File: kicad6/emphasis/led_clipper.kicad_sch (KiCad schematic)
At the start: 16 parts, among them U2 TL072

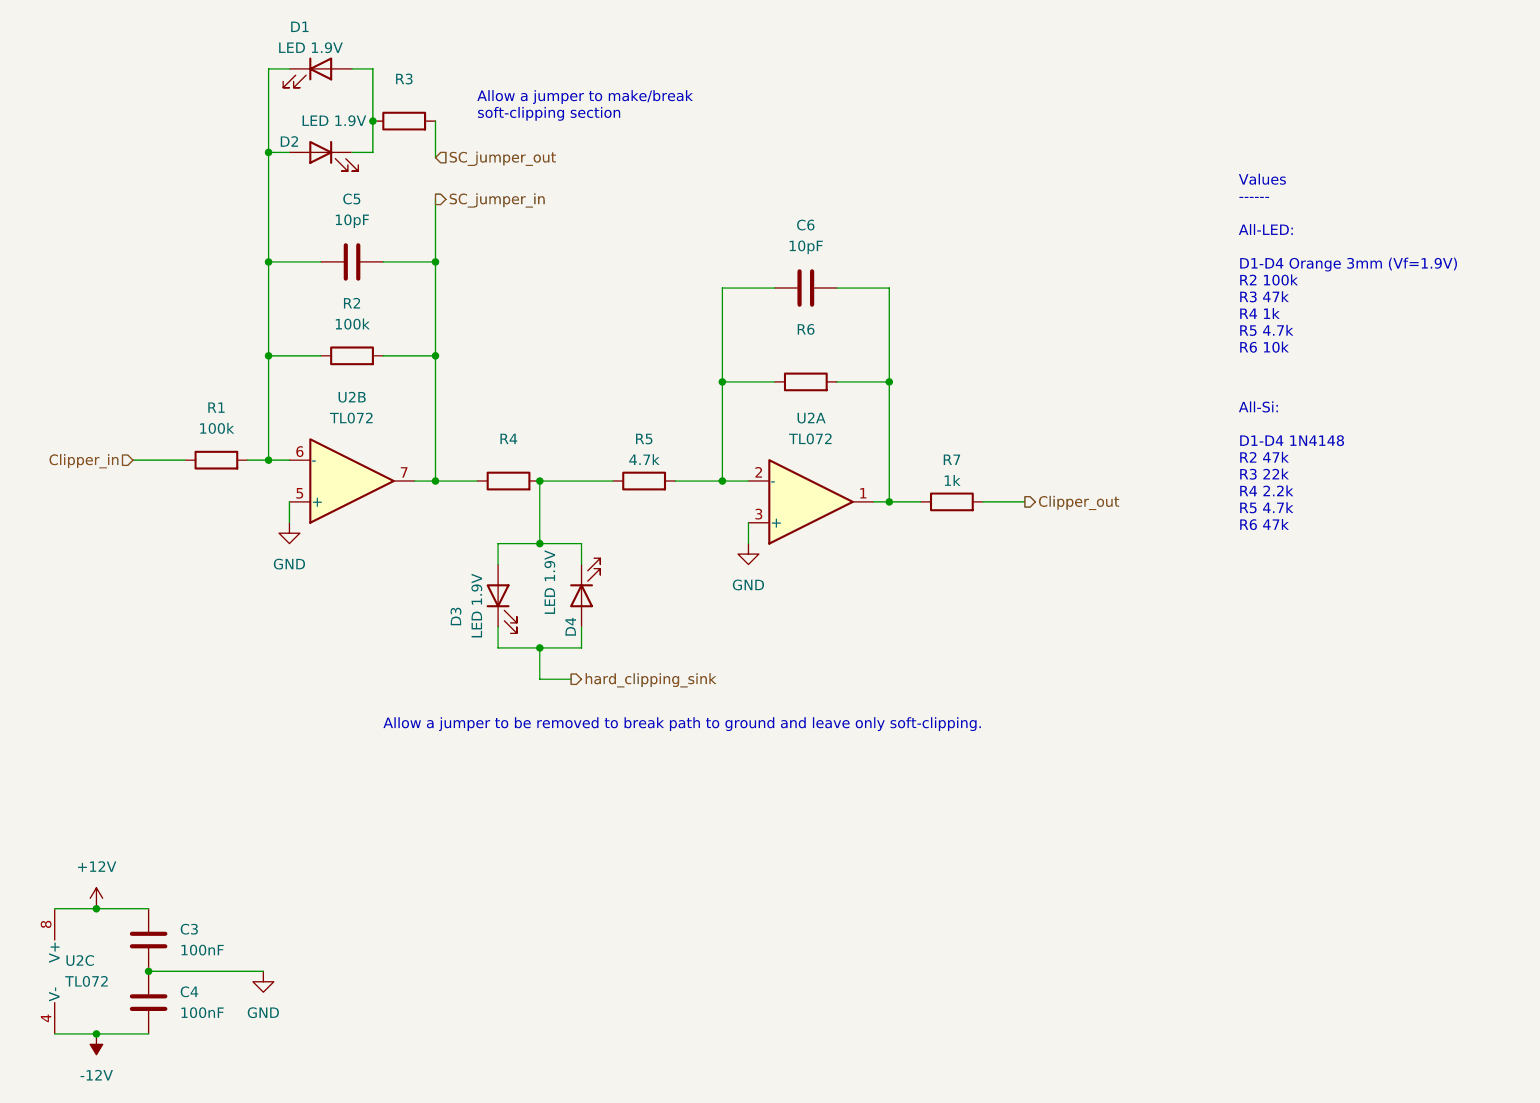
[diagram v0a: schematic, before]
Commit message: Emphasis: flipped board, take 1
Not entirely happy with the way this is going, might start again.

Basically I messed up the orientation of the main board relative to
the control board: to avoid having the patch_sm stick out the side,
parts need to be mounted on the "back" of main board. But this flips
the orientation of patch_sm and ICs, so everything needs to be
re-routed.
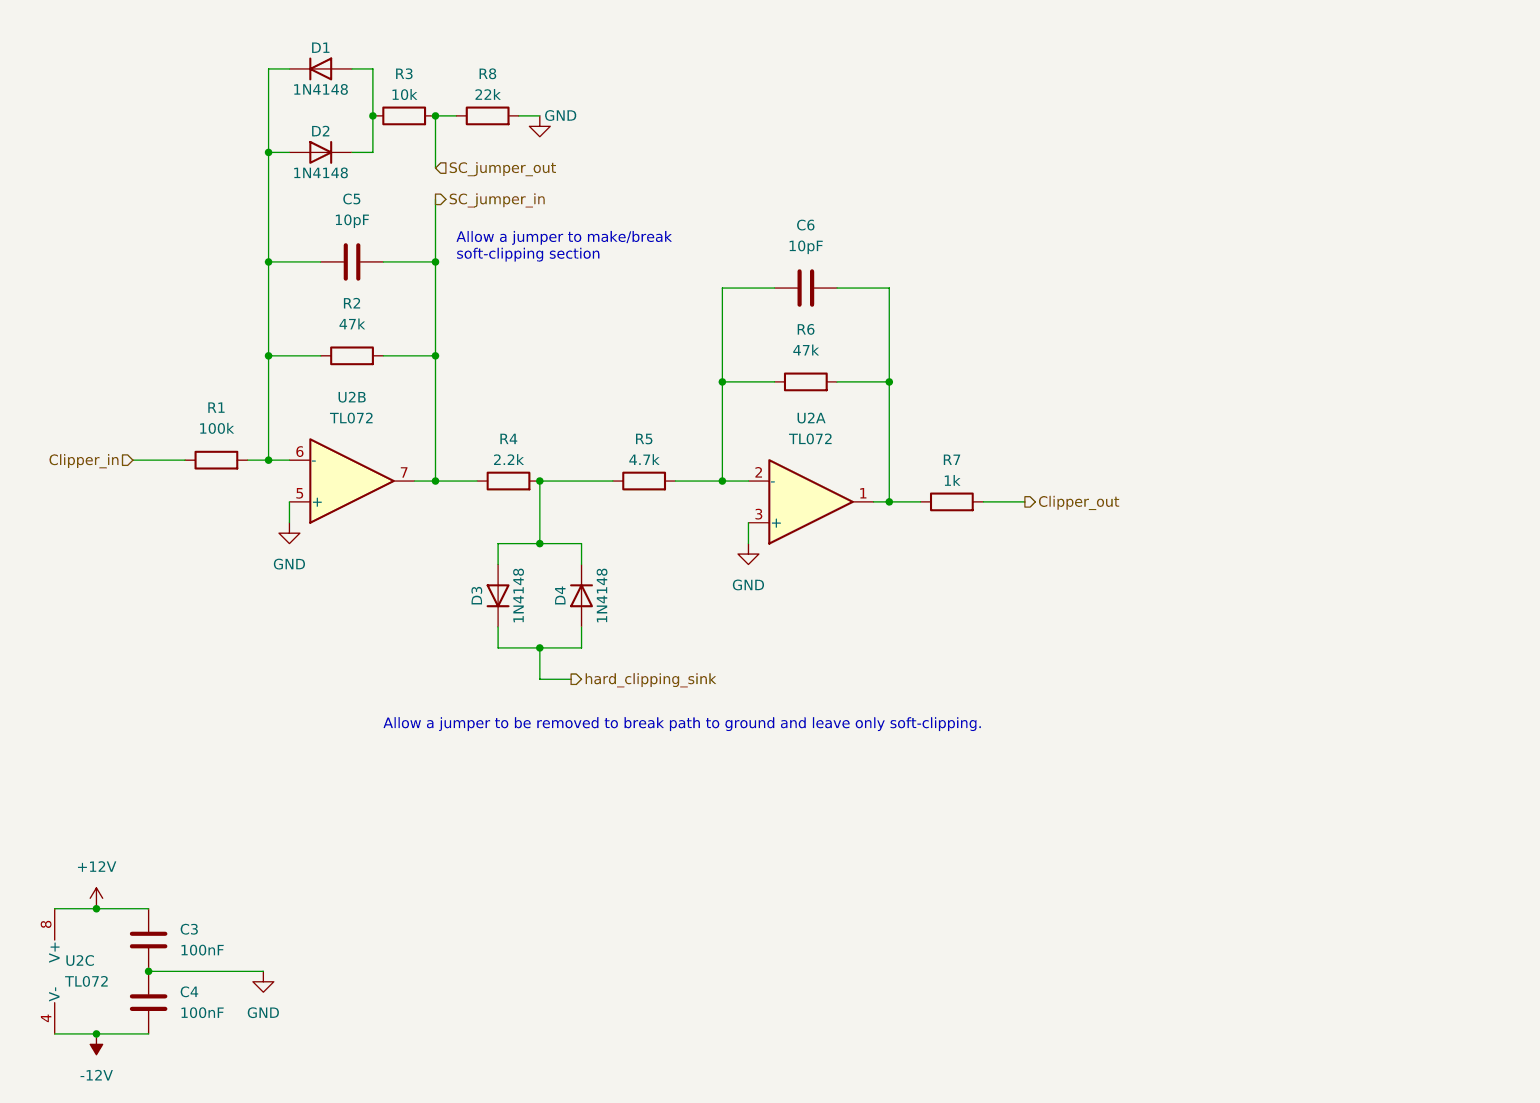
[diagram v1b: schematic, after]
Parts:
- added R8: 22k, Resistor_THT:R_Axial_DIN0207_L6.3mm_D2.5mm_P10.16mm_Horizontal, symbol Device:R
- D1, D2, D3, D4: value LED 1.9V -> 1N4148; footprint LED_THT:LED_D3.0mm_FlatTop -> Diode_THT:D_DO-35_SOD27_P7.62mm_Horizontal; symbol Device:LED -> Diode:1N4148
- R2: value 100k -> 47k
- R3: value (none) -> 10k; footprint (none) -> Resistor_THT:R_Axial_DIN0207_L6.3mm_D2.5mm_P10.16mm_Horizontal
- R4: value (none) -> 2.2k; footprint (none) -> Resistor_THT:R_Axial_DIN0207_L6.3mm_D2.5mm_P10.16mm_Horizontal
- R6: value (none) -> 47k; footprint (none) -> Resistor_THT:R_Axial_DIN0207_L6.3mm_D2.5mm_P10.16mm_Horizontal
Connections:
- net GND: now also R8.2
- net SC_jumper_out: now also R8.1
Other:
- note removed: "All-Si: D1-D4 1N4148 R2 47k R3 22k R4 2.2k R5 4.7k R6 47k"
- note removed: "Values ------ All-LED: D1-D4 Orange 3mm (Vf=1.9V) R2 100k R3 47k R4 1k R5 4.7k R6 10k"
- moved on the sheet: R3
